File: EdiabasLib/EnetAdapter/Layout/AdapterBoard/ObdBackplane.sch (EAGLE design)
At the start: 11 parts, among them J1 OBDII, U1 FPC-FFC-CONNECTOR-08-1MM, U2 FPC-FFC-CONNECTOR-08-1MM-L

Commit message: Using larger resistor
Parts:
- R1: device rcl:R-EU_R2010 -> resistor:R-EU_R2512
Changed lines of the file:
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@@
 <part name="J1" library="SparkFun-Connectors" deviceset="OBDII" device=""/>
 <part name="D1" library="diode" deviceset="DIODE-" device="DO214AC"/>
-<part name="R1" library="rcl" deviceset="R-EU_" device="R2010" value="511"/>
+<part name="R1" library="resistor" deviceset="R-EU_" device="R2512" value="511"/>
 <part name="FRAME1" library="frames" deviceset="DINA4_L" device=""/>
 <part name="GND1" library="supply1" deviceset="GND" device=""/>

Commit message: Layout for elecrow
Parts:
- removed U2: FPC-FFC-CONNECTOR-08-1MM-L, obd_special:FPC-FFC-CONNECTOR-08-1MM-L
- U1: value FPC-FFC-CONNECTOR-08-1MM -> FPC-FFC-CONNECTOR-08-1MM-L; device obd_special:FPC-FFC-CONNECTOR-08-1MM -> obd_special:FPC-FFC-CONNECTOR-08-1MM-L
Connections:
- net GND: no longer IN-.1
- net N$3: no longer U2.8
- net N$4: no longer U2.7
- net N$5: no longer U2.6
- net N$6: now also U1.3; no longer U1.5, U2.5
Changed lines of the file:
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@@
 <part name="POWER+" library="pinhead" deviceset="PINHD-1X1" device="_2.54" value="5V"/>
 <part name="POWER-" library="pinhead" deviceset="PINHD-1X1" device="_2.54" value="GND"/>
-<part name="U1" library="obd_special" deviceset="FPC-FFC-CONNECTOR-08-1MM" device="" value="FPC-FFC-CONNECTOR-08-1MM"/>
-<part name="U2" library="obd_special" deviceset="FPC-FFC-CONNECTOR-08-1MM-L" device="" value="FPC-FFC-CONNECTOR-08-1MM-L"/>
+<part name="U1" library="obd_special" deviceset="FPC-FFC-CONNECTOR-08-1MM-L" device="" value="FPC-FFC-CONNECTOR-08-1MM-L"/>
 </parts>
 <sheets>
@@
 <instance part="POWER-" gate="G$1" x="91.44" y="149.86"/>
 <instance part="U1" gate="A" x="-7.62" y="261.62"/>
-<instance part="U2" gate="A" x="55.88" y="261.62"/>
 </instances>
 <busses>
@@
 <junction x="88.9" y="170.18"/>
 <pinref part="POWER-" gate="G$1" pin="1"/>
-<pinref part="IN-" gate="G$1" pin="1"/>
-<wire x1="88.9" y1="180.34" x2="88.9" y2="210.82" width="0.1524" layer="91"/>
-<junction x="88.9" y="180.34"/>
 </segment>
 </net>
@@
 <wire x1="-30.48" y1="210.82" x2="-38.1" y2="210.82" width="0.1524" layer="91"/>
 <wire x1="-38.1" y1="210.82" x2="-38.1" y2="243.84" width="0.1524" layer="91"/>
-<wire x1="-38.1" y1="243.84" x2="12.7" y2="243.84" width="0.1524" layer="91"/>
+<wire x1="-38.1" y1="243.84" x2="15.24" y2="243.84" width="0.1524" layer="91"/>
 <pinref part="U1" gate="A" pin="8"/>
-<wire x1="12.7" y1="243.84" x2="76.2" y2="243.84" width="0.1524" layer="91"/>
-<wire x1="10.16" y1="256.54" x2="12.7" y2="256.54" width="0.1524" layer="91"/>
-<wire x1="12.7" y1="256.54" x2="12.7" y2="243.84" width="0.1524" layer="91"/>
-<junction x="12.7" y="243.84"/>
-<pinref part="U2" gate="A" pin="8"/>
-<wire x1="73.66" y1="256.54" x2="76.2" y2="256.54" width="0.1524" layer="91"/>
-<wire x1="76.2" y1="256.54" x2="76.2" y2="243.84" width="0.1524" layer="91"/>
+<wire x1="10.16" y1="256.54" x2="15.24" y2="256.54" width="0.1524" layer="91"/>
+<wire x1="15.24" y1="256.54" x2="15.24" y2="243.84" width="0.1524" layer="91"/>
 </segment>
 </net>
@@
 <pinref part="J1" gate="G$1" pin="11"/>
 <wire x1="15.24" y1="210.82" x2="22.86" y2="210.82" width="0.1524" layer="91"/>
-<wire x1="22.86" y1="210.82" x2="22.86" y2="241.3" width="0.1524" layer="91"/>
-<wire x1="22.86" y1="241.3" x2="-27.94" y2="241.3" width="0.1524" layer="91"/>
-<wire x1="22.86" y1="241.3" x2="35.56" y2="241.3" width="0.1524" layer="91"/>
-<junction x="22.86" y="241.3"/>
-<wire x1="35.56" y1="241.3" x2="35.56" y2="256.54" width="0.1524" layer="91"/>
-<pinref part="U2" gate="A" pin="7"/>
-<wire x1="35.56" y1="256.54" x2="38.1" y2="256.54" width="0.1524" layer="91"/>
+<wire x1="22.86" y1="210.82" x2="22.86" y2="228.6" width="0.1524" layer="91"/>
+<wire x1="22.86" y1="228.6" x2="-30.48" y2="228.6" width="0.1524" layer="91"/>
+<wire x1="-30.48" y1="228.6" x2="-30.48" y2="256.54" width="0.1524" layer="91"/>
 <pinref part="U1" gate="A" pin="7"/>
-<wire x1="-25.4" y1="256.54" x2="-27.94" y2="256.54" width="0.1524" layer="91"/>
-<wire x1="-27.94" y1="256.54" x2="-27.94" y2="241.3" width="0.1524" layer="91"/>
+<wire x1="-30.48" y1="256.54" x2="-25.4" y2="256.54" width="0.1524" layer="91"/>
 </segment>
 </net>
@@
 <pinref part="J1" gate="G$1" pin="12"/>
 <wire x1="15.24" y1="208.28" x2="25.4" y2="208.28" width="0.1524" layer="91"/>
-<wire x1="25.4" y1="208.28" x2="25.4" y2="236.22" width="0.1524" layer="91"/>
+<wire x1="25.4" y1="208.28" x2="25.4" y2="259.08" width="0.1524" layer="91"/>
 <pinref part="U1" gate="A" pin="6"/>
-<wire x1="25.4" y1="236.22" x2="25.4" y2="259.08" width="0.1524" layer="91"/>
 <wire x1="25.4" y1="259.08" x2="10.16" y2="259.08" width="0.1524" layer="91"/>
-<wire x1="25.4" y1="236.22" x2="81.28" y2="236.22" width="0.1524" layer="91"/>
-<junction x="25.4" y="236.22"/>
-<wire x1="81.28" y1="236.22" x2="81.28" y2="259.08" width="0.1524" layer="91"/>
-<pinref part="U2" gate="A" pin="6"/>
-<wire x1="81.28" y1="259.08" x2="73.66" y2="259.08" width="0.1524" layer="91"/>
 </segment>
 </net>
@@
 <segment>
 <pinref part="J1" gate="G$1" pin="13"/>
-<wire x1="15.24" y1="205.74" x2="27.94" y2="205.74" width="0.1524" layer="91"/>
-<wire x1="27.94" y1="205.74" x2="27.94" y2="238.76" width="0.1524" layer="91"/>
-<wire x1="27.94" y1="238.76" x2="-30.48" y2="238.76" width="0.1524" layer="91"/>
-<wire x1="-30.48" y1="238.76" x2="-30.48" y2="259.08" width="0.1524" layer="91"/>
-<pinref part="U1" gate="A" pin="5"/>
-<wire x1="-30.48" y1="259.08" x2="-25.4" y2="259.08" width="0.1524" layer="91"/>
-<wire x1="27.94" y1="238.76" x2="30.48" y2="238.76" width="0.1524" layer="91"/>
-<wire x1="30.48" y1="238.76" x2="30.48" y2="259.08" width="0.1524" layer="91"/>
-<junction x="27.94" y="238.76"/>
-<pinref part="U2" gate="A" pin="5"/>
-<wire x1="30.48" y1="259.08" x2="38.1" y2="259.08" width="0.1524" layer="91"/>
+<wire x1="15.24" y1="205.74" x2="20.32" y2="205.74" width="0.1524" layer="91"/>
+<pinref part="U1" gate="A" pin="3"/>
+<wire x1="-25.4" y1="261.62" x2="-33.02" y2="261.62" width="0.1524" layer="91"/>
+<wire x1="-33.02" y1="261.62" x2="-33.02" y2="226.06" width="0.1524" layer="91"/>
+<wire x1="-33.02" y1="226.06" x2="20.32" y2="226.06" width="0.1524" layer="91"/>
+<wire x1="20.32" y1="226.06" x2="20.32" y2="205.74" width="0.1524" layer="91"/>
 </segment>
 </net>

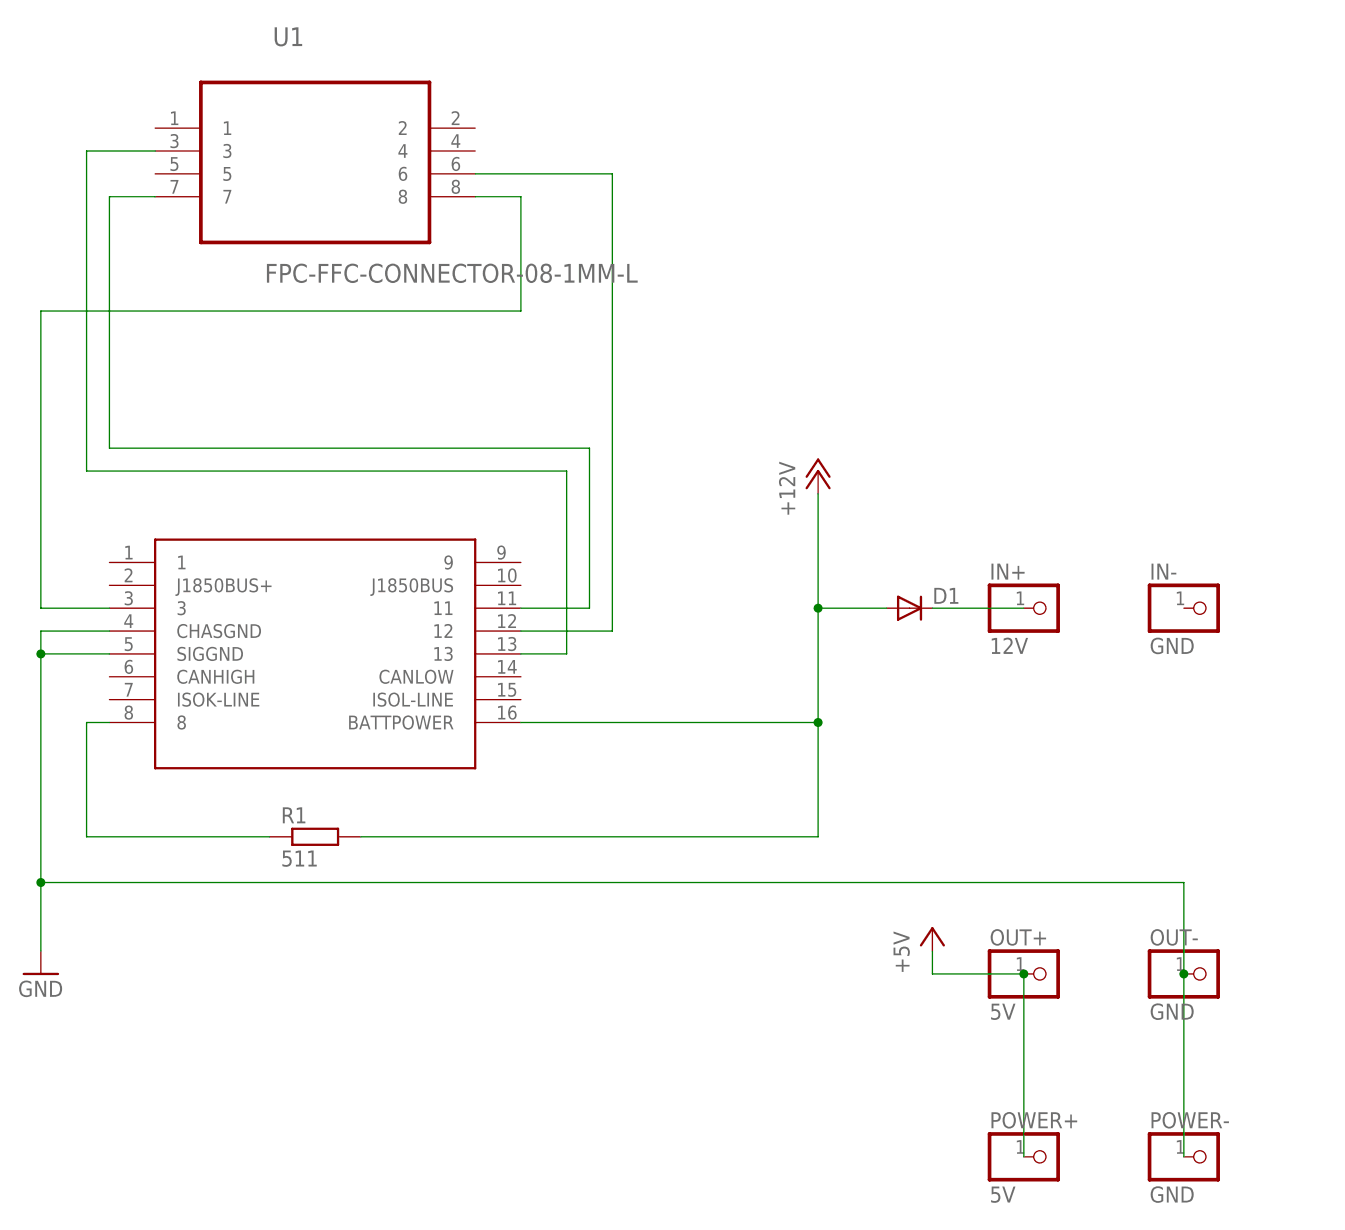
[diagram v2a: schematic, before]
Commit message: FFC connector replaced
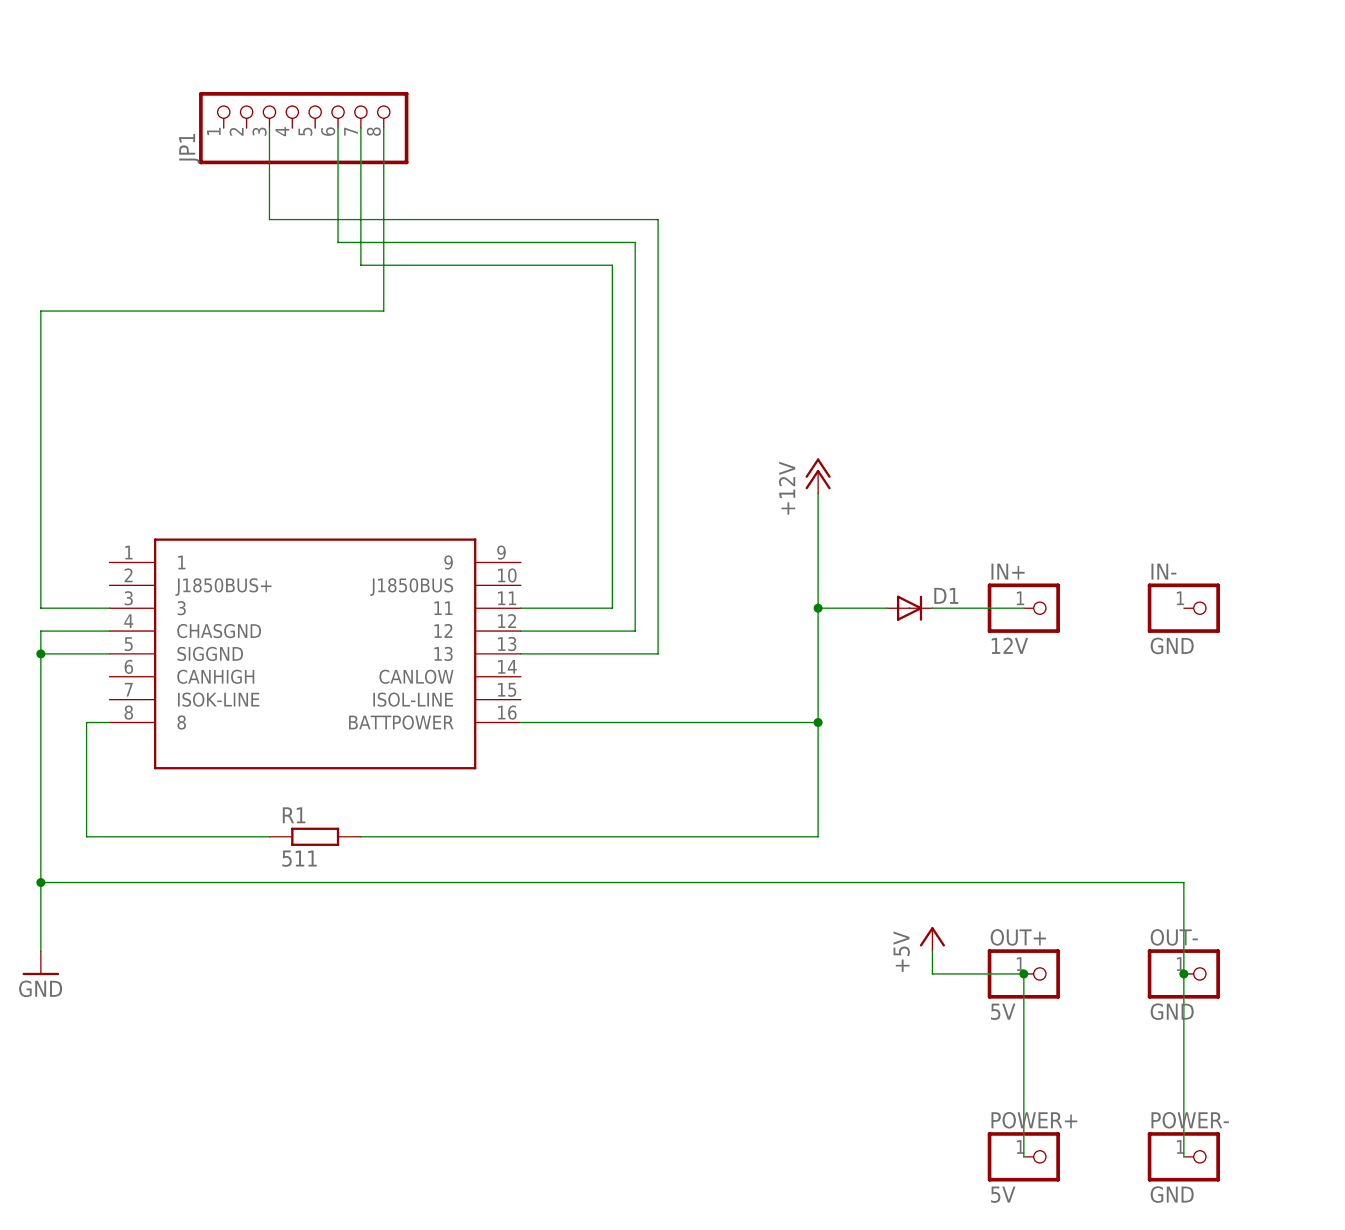
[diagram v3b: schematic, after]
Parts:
- removed U1: FPC-FFC-CONNECTOR-08-1MM-L, obd_special:FPC-FFC-CONNECTOR-08-1MM-L
- added JP1: (no value), obd_special:PINHD-1X8_1.00
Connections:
- removed net N$5: J1.12, U1.6
- new net N$7: J1.11, JP1.7
- net N$3: now also JP1.8; no longer U1.8
- net N$4: now also J1.12, JP1.6; no longer J1.11, U1.7
- net N$6: now also JP1.3; no longer U1.3
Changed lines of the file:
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@@
 <part name="POWER+" library="pinhead" deviceset="PINHD-1X1" device="_2.54" value="5V"/>
 <part name="POWER-" library="pinhead" deviceset="PINHD-1X1" device="_2.54" value="GND"/>
-<part name="U1" library="obd_special" deviceset="FPC-FFC-CONNECTOR-08-1MM-L" device="" value="FPC-FFC-CONNECTOR-08-1MM-L"/>
+<part name="JP1" library="obd_special" deviceset="PINHD-1X8" device="_1.00"/>
 </parts>
 <sheets>
@@
 <instance part="POWER+" gate="G$1" x="73.66" y="149.86"/>
 <instance part="POWER-" gate="G$1" x="91.44" y="149.86"/>
-<instance part="U1" gate="A" x="-7.62" y="261.62"/>
+<instance part="JP1" gate="A" x="-7.62" y="266.7" rot="R90"/>
 </instances>
 <busses>
@@
 <wire x1="-30.48" y1="210.82" x2="-38.1" y2="210.82" width="0.1524" layer="91"/>
 <wire x1="-38.1" y1="210.82" x2="-38.1" y2="243.84" width="0.1524" layer="91"/>
-<wire x1="-38.1" y1="243.84" x2="15.24" y2="243.84" width="0.1524" layer="91"/>
-<pinref part="U1" gate="A" pin="8"/>
-<wire x1="10.16" y1="256.54" x2="15.24" y2="256.54" width="0.1524" layer="91"/>
-<wire x1="15.24" y1="256.54" x2="15.24" y2="243.84" width="0.1524" layer="91"/>
-</segment>
-</net>
-<net name="N$4" class="0">
-<segment>
-<pinref part="J1" gate="G$1" pin="11"/>
-<wire x1="15.24" y1="210.82" x2="22.86" y2="210.82" width="0.1524" layer="91"/>
-<wire x1="22.86" y1="210.82" x2="22.86" y2="228.6" width="0.1524" layer="91"/>
-<wire x1="22.86" y1="228.6" x2="-30.48" y2="228.6" width="0.1524" layer="91"/>
-<wire x1="-30.48" y1="228.6" x2="-30.48" y2="256.54" width="0.1524" layer="91"/>
-<pinref part="U1" gate="A" pin="7"/>
-<wire x1="-30.48" y1="256.54" x2="-25.4" y2="256.54" width="0.1524" layer="91"/>
-</segment>
-</net>
-<net name="N$5" class="0">
-<segment>
-<pinref part="J1" gate="G$1" pin="12"/>
-<wire x1="15.24" y1="208.28" x2="25.4" y2="208.28" width="0.1524" layer="91"/>
-<wire x1="25.4" y1="208.28" x2="25.4" y2="259.08" width="0.1524" layer="91"/>
-<pinref part="U1" gate="A" pin="6"/>
-<wire x1="25.4" y1="259.08" x2="10.16" y2="259.08" width="0.1524" layer="91"/>
+<wire x1="-38.1" y1="243.84" x2="0" y2="243.84" width="0.1524" layer="91"/>
+<pinref part="JP1" gate="A" pin="8"/>
+<wire x1="0" y1="243.84" x2="0" y2="264.16" width="0.1524" layer="91"/>
 </segment>
 </net>
@@
 <segment>
 <pinref part="J1" gate="G$1" pin="13"/>
-<wire x1="15.24" y1="205.74" x2="20.32" y2="205.74" width="0.1524" layer="91"/>
-<pinref part="U1" gate="A" pin="3"/>
-<wire x1="-25.4" y1="261.62" x2="-33.02" y2="261.62" width="0.1524" layer="91"/>
-<wire x1="-33.02" y1="261.62" x2="-33.02" y2="226.06" width="0.1524" layer="91"/>
-<wire x1="-33.02" y1="226.06" x2="20.32" y2="226.06" width="0.1524" layer="91"/>
-<wire x1="20.32" y1="226.06" x2="20.32" y2="205.74" width="0.1524" layer="91"/>
+<wire x1="15.24" y1="205.74" x2="30.48" y2="205.74" width="0.1524" layer="91"/>
+<wire x1="30.48" y1="205.74" x2="30.48" y2="254" width="0.1524" layer="91"/>
+<wire x1="30.48" y1="254" x2="-12.7" y2="254" width="0.1524" layer="91"/>
+<pinref part="JP1" gate="A" pin="3"/>
+<wire x1="-12.7" y1="254" x2="-12.7" y2="264.16" width="0.1524" layer="91"/>
 </segment>
 </net>
+<net name="N$7" class="0">
+<segment>
+<pinref part="J1" gate="G$1" pin="11"/>
+<wire x1="15.24" y1="210.82" x2="25.4" y2="210.82" width="0.1524" layer="91"/>
+<wire x1="25.4" y1="210.82" x2="25.4" y2="248.92" width="0.1524" layer="91"/>
+<wire x1="25.4" y1="248.92" x2="-2.54" y2="248.92" width="0.1524" layer="91"/>
+<pinref part="JP1" gate="A" pin="7"/>
+<wire x1="-2.54" y1="248.92" x2="-2.54" y2="264.16" width="0.1524" layer="91"/>
+</segment>
+</net>
+<net name="N$4" class="0">
+<segment>
+<pinref part="J1" gate="G$1" pin="12"/>
+<wire x1="15.24" y1="208.28" x2="27.94" y2="208.28" width="0.1524" layer="91"/>
+<wire x1="27.94" y1="208.28" x2="27.94" y2="251.46" width="0.1524" layer="91"/>
+<wire x1="27.94" y1="251.46" x2="-5.08" y2="251.46" width="0.1524" layer="91"/>
+<pinref part="JP1" gate="A" pin="6"/>
+<wire x1="-5.08" y1="251.46" x2="-5.08" y2="264.16" width="0.1524" layer="91"/>
+</segment>
+</net>

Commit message: Connector layout improved
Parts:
- JP1: value (none) -> ETHERNET
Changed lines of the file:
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@@
 <part name="POWER+" library="pinhead" deviceset="PINHD-1X1" device="_2.54" value="5V"/>
 <part name="POWER-" library="pinhead" deviceset="PINHD-1X1" device="_2.54" value="GND"/>
-<part name="JP1" library="obd_special" deviceset="PINHD-1X8" device="_1.00"/>
+<part name="JP1" library="obd_special" deviceset="PINHD-1X8" device="_1.00" value="ETHERNET"/>
 </parts>
 <sheets>

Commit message: Layout improved
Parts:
- renumbered J1 to OBDII, POWER+ to P+, POWER- to P-
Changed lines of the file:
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@@
 </classes>
 <parts>
-<part name="J1" library="SparkFun-Connectors" deviceset="OBDII" device=""/>
+<part name="OBDII" library="SparkFun-Connectors" deviceset="OBDII" device=""/>
 <part name="D1" library="diode" deviceset="DIODE-" device="DO214AC"/>
 <part name="R1" library="resistor" deviceset="R-EU_" device="R2512" value="511"/>
@@
 <part name="OUT-" library="pinhead" deviceset="PINHD-1X1" device="_2.54" value="GND"/>
 <part name="P+2" library="supply1" deviceset="+5V" device=""/>
-<part name="POWER+" library="pinhead" deviceset="PINHD-1X1" device="_2.54" value="5V"/>
-<part name="POWER-" library="pinhead" deviceset="PINHD-1X1" device="_2.54" value="GND"/>
+<part name="P+" library="pinhead" deviceset="PINHD-1X1" device="_2.54" value="5V"/>
+<part name="P-" library="pinhead" deviceset="PINHD-1X1" device="_2.54" value="GND"/>
 <part name="JP1" library="obd_special" deviceset="PINHD-1X8" device="_1.00" value="ETHERNET"/>
 </parts>
@@
 </plain>
 <instances>
-<instance part="J1" gate="G$1" x="-7.62" y="205.74"/>
+<instance part="OBDII" gate="G$1" x="-7.62" y="205.74"/>
 <instance part="D1" gate="G$1" x="58.42" y="210.82"/>
 <instance part="R1" gate="G$1" x="-7.62" y="185.42"/>
@@
 <instance part="OUT-" gate="G$1" x="91.44" y="170.18"/>
 <instance part="P+2" gate="1" x="60.96" y="175.26"/>
-<instance part="POWER+" gate="G$1" x="73.66" y="149.86"/>
-<instance part="POWER-" gate="G$1" x="91.44" y="149.86"/>
+<instance part="P+" gate="G$1" x="73.66" y="149.86"/>
+<instance part="P-" gate="G$1" x="91.44" y="149.86"/>
 <instance part="JP1" gate="A" x="-7.62" y="266.7" rot="R90"/>
 </instances>
@@
 <net name="GND" class="0">
 <segment>
-<pinref part="J1" gate="G$1" pin="SIGGND"/>
-<pinref part="J1" gate="G$1" pin="CHASGND"/>
+<pinref part="OBDII" gate="G$1" pin="SIGGND"/>
+<pinref part="OBDII" gate="G$1" pin="CHASGND"/>
 <wire x1="-30.48" y1="208.28" x2="-38.1" y2="208.28" width="0.1524" layer="91"/>
 <wire x1="-38.1" y1="208.28" x2="-38.1" y2="205.74" width="0.1524" layer="91"/>
@@
 <wire x1="88.9" y1="170.18" x2="88.9" y2="149.86" width="0.1524" layer="91"/>
 <junction x="88.9" y="170.18"/>
-<pinref part="POWER-" gate="G$1" pin="1"/>
+<pinref part="P-" gate="G$1" pin="1"/>
 </segment>
 </net>
@@
 <segment>
 <pinref part="P+1" gate="1" pin="+12V"/>
-<pinref part="J1" gate="G$1" pin="BATTPOWER"/>
+<pinref part="OBDII" gate="G$1" pin="BATTPOWER"/>
 <wire x1="48.26" y1="223.52" x2="48.26" y2="210.82" width="0.1524" layer="91"/>
 <wire x1="48.26" y1="210.82" x2="48.26" y2="198.12" width="0.1524" layer="91"/>
@@
 <net name="N$2" class="0">
 <segment>
-<pinref part="J1" gate="G$1" pin="8"/>
+<pinref part="OBDII" gate="G$1" pin="8"/>
 <wire x1="-30.48" y1="198.12" x2="-33.02" y2="198.12" width="0.1524" layer="91"/>
 <wire x1="-33.02" y1="198.12" x2="-33.02" y2="185.42" width="0.1524" layer="91"/>
@@
 <wire x1="71.12" y1="170.18" x2="71.12" y2="149.86" width="0.1524" layer="91"/>
 <junction x="71.12" y="170.18"/>
-<pinref part="POWER+" gate="G$1" pin="1"/>
+<pinref part="P+" gate="G$1" pin="1"/>
 </segment>
 </net>
 <net name="N$3" class="0">
 <segment>
-<pinref part="J1" gate="G$1" pin="3"/>
+<pinref part="OBDII" gate="G$1" pin="3"/>
 <wire x1="-30.48" y1="210.82" x2="-38.1" y2="210.82" width="0.1524" layer="91"/>
 <wire x1="-38.1" y1="210.82" x2="-38.1" y2="243.84" width="0.1524" layer="91"/>
@@
 <net name="N$6" class="0">
 <segment>
-<pinref part="J1" gate="G$1" pin="13"/>
+<pinref part="OBDII" gate="G$1" pin="13"/>
 <wire x1="15.24" y1="205.74" x2="30.48" y2="205.74" width="0.1524" layer="91"/>
 <wire x1="30.48" y1="205.74" x2="30.48" y2="254" width="0.1524" layer="91"/>
@@
 <net name="N$7" class="0">
 <segment>
-<pinref part="J1" gate="G$1" pin="11"/>
+<pinref part="OBDII" gate="G$1" pin="11"/>
 <wire x1="15.24" y1="210.82" x2="25.4" y2="210.82" width="0.1524" layer="91"/>
 <wire x1="25.4" y1="210.82" x2="25.4" y2="248.92" width="0.1524" layer="91"/>
@@
 <net name="N$4" class="0">
 <segment>
-<pinref part="J1" gate="G$1" pin="12"/>
+<pinref part="OBDII" gate="G$1" pin="12"/>
 <wire x1="15.24" y1="208.28" x2="27.94" y2="208.28" width="0.1524" layer="91"/>
 <wire x1="27.94" y1="208.28" x2="27.94" y2="251.46" width="0.1524" layer="91"/>
